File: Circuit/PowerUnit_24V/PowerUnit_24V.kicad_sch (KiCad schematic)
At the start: 49 parts, among them J1 Conn_01x02_Pin, J10 Conn_01x04_Pin, J12 Conn_01x02_Pin, J13 Conn_01x02_Pin, J19 Conn_01x02_Pin, J2 Conn_01x02_Pin, J3 Conn_01x02_Pin, J4 Conn_01x02_Pin, J5 Conn_01x02_Pin, J6 Conn_01x02_Pin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

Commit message: 24V基板完成
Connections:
- net +24V_CTRL: no longer R3.1
- net GND: now also J6.1 (Pin_1), J7.1 (Pin_1), J8.1 (Pin_1), J9.1 (Pin_1); no longer D3.1 (K)
- net GNDPWR: now also D3.1 (K); no longer J6.1 (Pin_1), J7.1 (Pin_1), J8.1 (Pin_1), J9.1 (Pin_1)
- net Vsense1: now reaches J12.2 (Pin_2), J13.1 (Pin_1), K1.87, R5.1
- net Vsense1: now also R3.1; no longer R7.1
- net at F1.2, R5.4: now also R7.1
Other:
- moved on the sheet: D3, R3, R7

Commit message: 24V基板とメインモータ基板を修正
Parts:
- J2, J3, J4, J5: footprint Connector_AMASS:AMASS_XT60-M_1x02_P7.20mm_Vertical -> OU_Conn:AMASS_XT60-F
- J6, J7, J8, J9: footprint OU_Conn:XT30U-M -> OU_Conn:AMASS_XT30U-F
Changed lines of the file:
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@@
 			)
 		)
-		(property "Footprint" "OU_Conn:XT30U-M"
+		(property "Footprint" "OU_Conn:AMASS_XT30U-F"
 			(at 101.6 144.78 0)
 			(hide yes)
@@
 			)
 		)
-		(property "Footprint" "Connector_AMASS:AMASS_XT60-M_1x02_P7.20mm_Vertical"
+		(property "Footprint" "OU_Conn:AMASS_XT60-F"
 			(at 58.42 144.78 0)
 			(hide yes)
@@
 			)
 		)
-		(property "Footprint" "OU_Conn:XT30U-M"
+		(property "Footprint" "OU_Conn:AMASS_XT30U-F"
 			(at 134.62 144.78 0)
 			(hide yes)
@@
 			)
 		)
-		(property "Footprint" "Connector_AMASS:AMASS_XT60-M_1x02_P7.20mm_Vertical"
+		(property "Footprint" "OU_Conn:AMASS_XT60-F"
 			(at 38.1 144.78 0)
 			(hide yes)
@@
 			)
 		)
-		(property "Footprint" "OU_Conn:XT30U-M"
+		(property "Footprint" "OU_Conn:AMASS_XT30U-F"
 			(at 124.46 144.78 0)
 			(hide yes)
@@
 			)
 		)
-		(property "Footprint" "OU_Conn:XT30U-M"
+		(property "Footprint" "OU_Conn:AMASS_XT30U-F"
 			(at 113.03 144.78 0)
 			(hide yes)
@@
 			)
 		)
-		(property "Footprint" "Connector_AMASS:AMASS_XT60-M_1x02_P7.20mm_Vertical"
+		(property "Footprint" "OU_Conn:AMASS_XT60-F"
 			(at 68.58 144.78 0)
 			(hide yes)
@@
 			)
 		)
-		(property "Footprint" "Connector_AMASS:AMASS_XT60-M_1x02_P7.20mm_Vertical"
+		(property "Footprint" "OU_Conn:AMASS_XT60-F"
 			(at 48.26 144.78 0)
 			(hide yes)

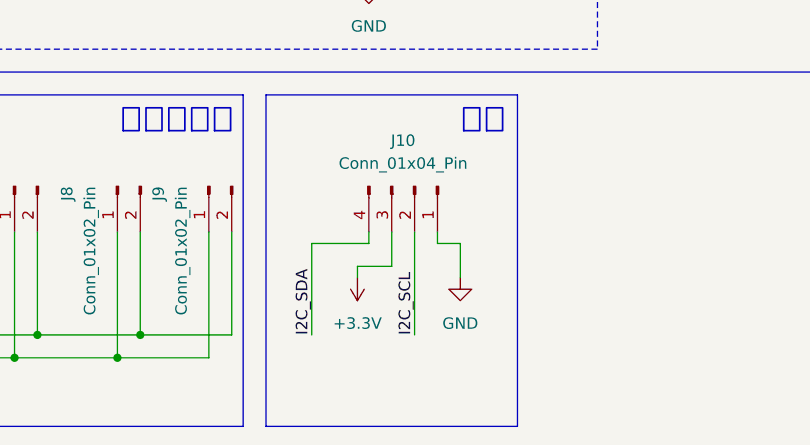
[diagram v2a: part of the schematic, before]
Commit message: Geminiに確認してもらって一部修正
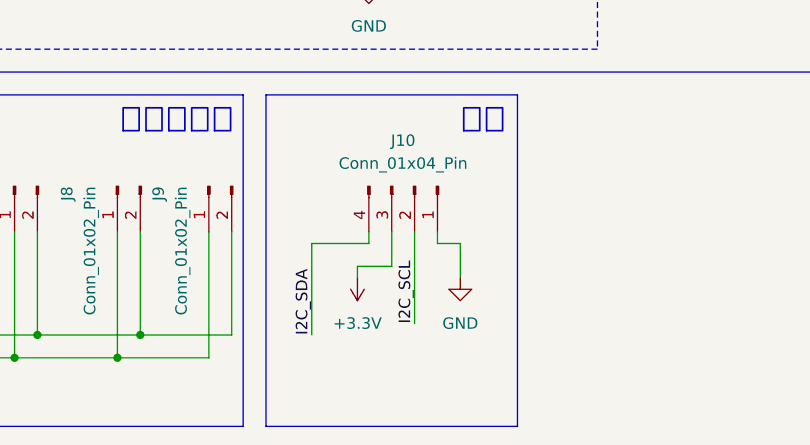
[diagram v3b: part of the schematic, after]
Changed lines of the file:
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@@
 	(wire
 		(pts
-			(xy 157.48 149.86) (xy 157.48 161.29)
+			(xy 157.48 149.86) (xy 157.48 160.02)
 		)
 		(stroke
@@
 	)
 	(label "I2C_SCL"
-		(at 157.48 161.29 90)
+		(at 157.48 160.02 90)
 		(effects
 			(font

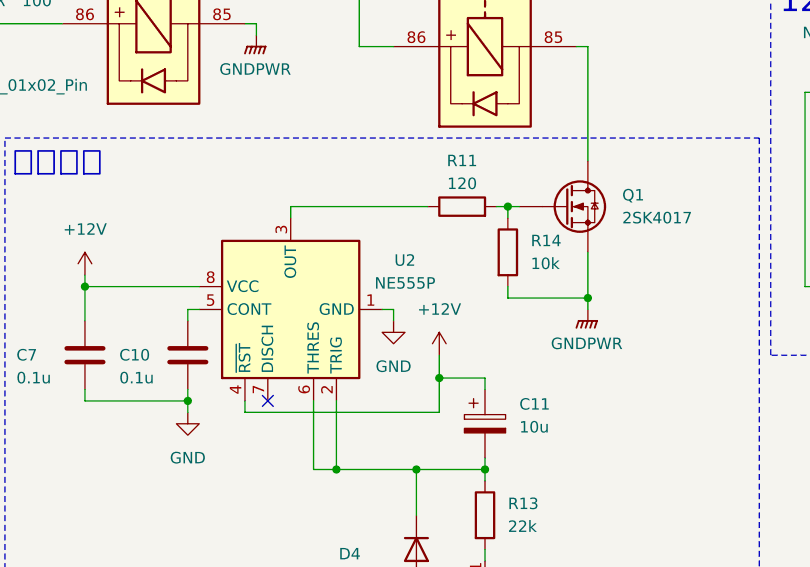
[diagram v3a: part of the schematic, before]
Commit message: 発注用データを用意 発注した
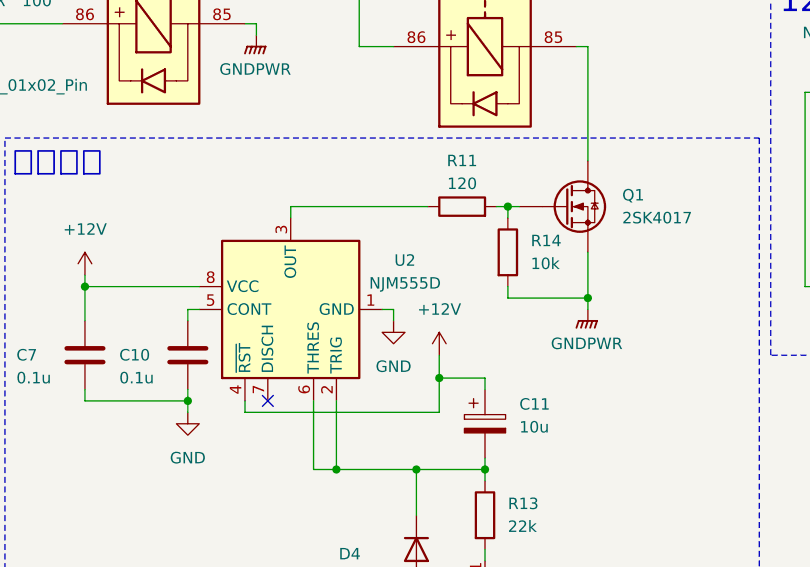
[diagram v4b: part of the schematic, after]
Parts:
- D3, D5, D6: MPN_URL (none) -> https://akizukidenshi.com/catalog/g/g111333/
- D4: MPN_URL (none) -> https://akizukidenshi.com/catalog/g/g100941/
- J1: MPN_URL (none) -> https://akizukidenshi.com/catalog/g/g118156/
- J2, J3, J4, J5: MPN_URL (none) -> https://akizukidenshi.com/catalog/g/g117952/
- J6, J7, J8, J9: MPN_URL (none) -> https://akizukidenshi.com/catalog/g/g117950/
- R10, R7, R9: MPN_URL (none) -> https://akizukidenshi.com/catalog/g/g125752/
- U2: value NE555P -> NJM555D; MPN_URL (none) -> https://akizukidenshi.com/catalog/g/g114531/
- U3: MPN_URL (none) -> https://akizukidenshi.com/catalog/g/g100163/
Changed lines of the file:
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@@
 			)
 		)
+		(property "MPN_URL" "https://akizukidenshi.com/catalog/g/g117950/"
+			(at 101.6 144.78 0)
+			(hide yes)
+			(show_name no)
+			(do_not_autoplace no)
+			(effects
+				(font
+					(size 1.27 1.27)
+				)
+			)
+		)
 		(pin "1"
 		)
@@
 			)
 		)
+		(property "MPN_URL" "https://akizukidenshi.com/catalog/g/g125752/"
+			(at 49.53 43.18 90)
+			(hide yes)
+			(show_name no)
+			(do_not_autoplace no)
+			(effects
+				(font
+					(size 1.27 1.27)
+				)
+			)
+		)
 		(pin "1"
 		)
@@
 			)
 		)
+		(property "MPN_URL" "https://akizukidenshi.com/catalog/g/g117952/"
+			(at 58.42 144.78 0)
+			(hide yes)
+			(show_name no)
+			(do_not_autoplace no)
+			(effects
+				(font
+					(size 1.27 1.27)
+				)
+			)
+		)
 		(pin "1"
 		)
@@
 			)
 		)
+		(property "MPN_URL" "https://akizukidenshi.com/catalog/g/g111333/"
+			(at 49.53 52.07 90)
+			(hide yes)
+			(show_name no)
+			(do_not_autoplace no)
+			(effects
+				(font
+					(size 1.27 1.27)
+				)
+			)
+		)
 		(pin "1"
 		)
@@
 			)
 		)
+		(property "MPN_URL" "https://akizukidenshi.com/catalog/g/g100941/"
+			(at 139.7 109.22 90)
+			(hide yes)
+			(show_name no)
+			(do_not_autoplace no)
+			(effects
+				(font
+					(size 1.27 1.27)
+				)
+			)
+		)
 		(pin "2"
 		)
@@
 			)
 		)
+		(property "MPN_URL" "https://akizukidenshi.com/catalog/g/g125752/"
+			(at 83.82 148.59 90)
+			(hide yes)
+			(show_name no)
+			(do_not_autoplace no)
+			(effects
+				(font
+					(size 1.27 1.27)
+				)
+			)
+		)
 		(pin "1"
 		)
@@
 			)
 		)
+		(property "MPN_URL" "https://akizukidenshi.com/catalog/g/g117950/"
+			(at 134.62 144.78 0)
+			(hide yes)
+			(show_name no)
+			(do_not_autoplace no)
+			(effects
+				(font
+					(size 1.27 1.27)
+				)
+			)
+		)
 		(pin "1"
 		)
@@
 			)
 		)
+		(property "MPN_URL" "https://akizukidenshi.com/catalog/g/g111333/"
+			(at 83.82 157.48 90)
+			(hide yes)
+			(show_name no)
+			(do_not_autoplace no)
+			(effects
+				(font
+					(size 1.27 1.27)
+				)
+			)
+		)
 		(pin "1"
 		)
@@
 			)
 		)
+		(property "MPN_URL" "https://akizukidenshi.com/catalog/g/g117952/"
+			(at 38.1 144.78 0)
+			(hide yes)
+			(show_name no)
+			(do_not_autoplace no)
+			(effects
+				(font
+					(size 1.27 1.27)
+				)
+			)
+		)
 		(pin "1"
 		)
@@
 			)
 		)
+		(property "MPN_URL" "https://akizukidenshi.com/catalog/g/g100163/"
+			(at 195.58 58.42 90)
+			(hide yes)
+			(show_name no)
+			(do_not_autoplace no)
+			(effects
+				(font
+					(size 1.27 1.27)
+				)
+			)
+		)
 		(pin "3"
 		)
@@
 			)
 		)
+		(property "MPN_URL" "https://akizukidenshi.com/catalog/g/g125752/"
+			(at 20.32 148.59 90)
+			(hide yes)
+			(show_name no)
+			(do_not_autoplace no)
+			(effects
+				(font
+					(size 1.27 1.27)
+				)
+			)
+		)
 		(pin "1"
 		)
@@
 			)
 		)
+		(property "MPN_URL" "https://akizukidenshi.com/catalog/g/g117950/"
+			(at 124.46 144.78 0)
+			(hide yes)
+			(show_name no)
+			(do_not_autoplace no)
+			(effects
+				(font
+					(size 1.27 1.27)
+				)
+			)
+		)
 		(pin "1"
 		)
@@
 			)
 		)
+		(property "MPN_URL" "https://akizukidenshi.com/catalog/g/g117950/"
+			(at 113.03 144.78 0)
+			(hide yes)
+			(show_name no)
+			(do_not_autoplace no)
+			(effects
+				(font
+					(size 1.27 1.27)
+				)
+			)
+		)
 		(pin "1"
 		)
@@
 			)
 		)
-		(property "Value" "NE555P"
+		(property "Value" "NJM555D"
 			(at 138.43 79.6446 90)
 			(show_name no)
@@
 			)
 		)
+		(property "MPN_URL" "https://akizukidenshi.com/catalog/g/g114531/"
+			(at 125.73 82.55 90)
+			(hide yes)
+			(show_name no)
+			(do_not_autoplace no)
+			(effects
+				(font
+					(size 1.27 1.27)
+				)
+			)
+		)
 		(pin "2"
 		)
@@
 			)
 		)
+		(property "MPN_URL" "https://akizukidenshi.com/catalog/g/g111333/"
+			(at 20.32 157.48 90)
+			(hide yes)
+			(show_name no)
+			(do_not_autoplace no)
+			(effects
+				(font
+					(size 1.27 1.27)
+				)
+			)
+		)
 		(pin "1"
 		)
@@
 			)
 		)
+		(property "MPN_URL" "https://akizukidenshi.com/catalog/g/g118156/"
+			(at 24.13 40.64 0)
+			(hide yes)
+			(show_name no)
+			(do_not_autoplace no)
+			(effects
+				(font
+					(size 1.27 1.27)
+				)
+			)
+		)
 		(pin "1"
 		)
@@
 			)
 		)
+		(property "MPN_URL" "https://akizukidenshi.com/catalog/g/g117952/"
+			(at 68.58 144.78 0)
+			(hide yes)
+			(show_name no)
+			(do_not_autoplace no)
+			(effects
+				(font
+					(size 1.27 1.27)
+				)
+			)
+		)
 		(pin "1"
 		)
@@
 			(at 48.26 144.78 0)
 			(hide yes)
+			(show_name no)
+			(do_not_autoplace no)
+			(effects
+				(font
+					(size 1.27 1.27)
+				)
+			)
+		)
+		(property "MPN_URL" "https://akizukidenshi.com/catalog/g/g117952/"
+			(at 48.26 144.78 0)
+			(hide yes)
